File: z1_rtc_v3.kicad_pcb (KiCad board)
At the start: 2 copper layers, 62.5 x 51 mm, 63 parts, among them J1 Conn_01x05, J10 Conn_01x02, J2 61200621621, J3 Conn_01x11, J4 Conn_01x11, J5 Conn_01x11, J6 Conn_01x11, J7 691137710002, J8 USB_B_Micro, J9 Conn_01x02, U1 LCMXO2-1200HC-4SG32C, U2 ATmega328PB-AU, U3 FT230XS, Y1 Crystal_Small

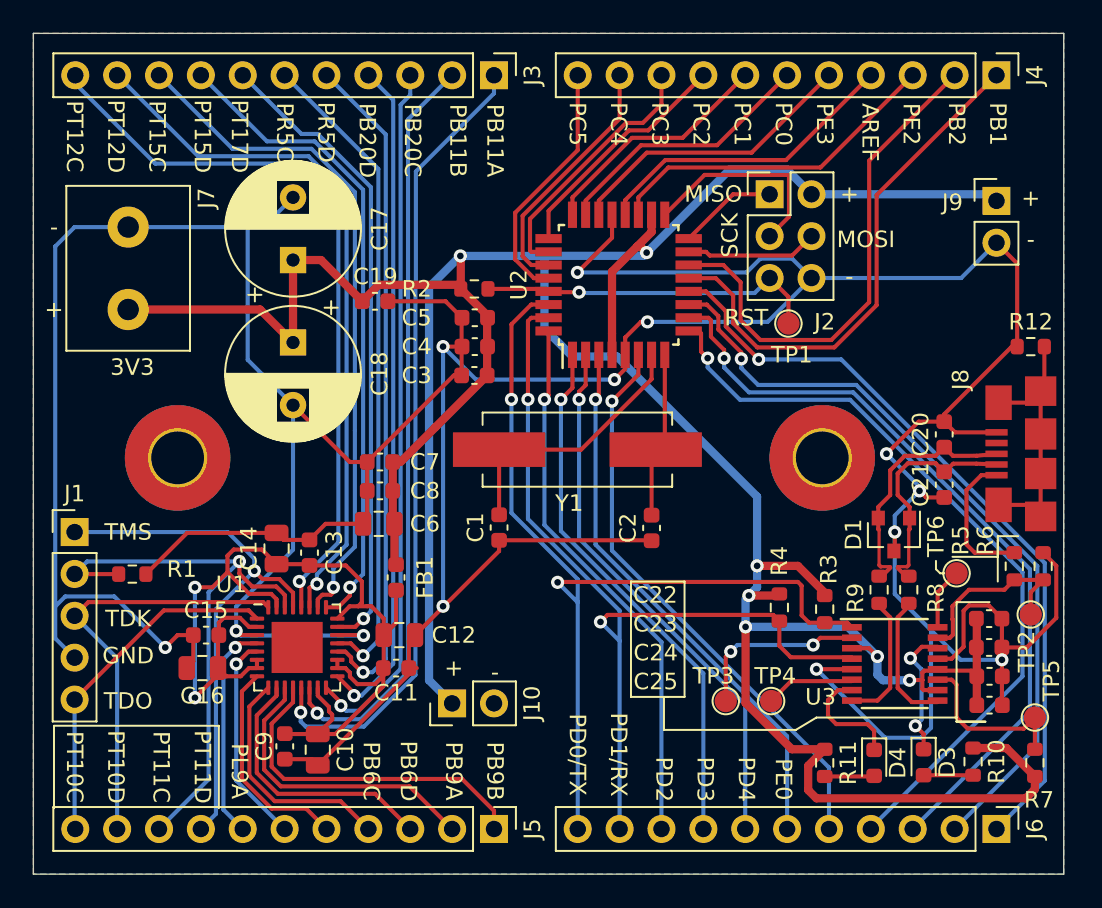
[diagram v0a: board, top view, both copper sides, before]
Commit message: board files for v3.2, with the tinyFPGA module
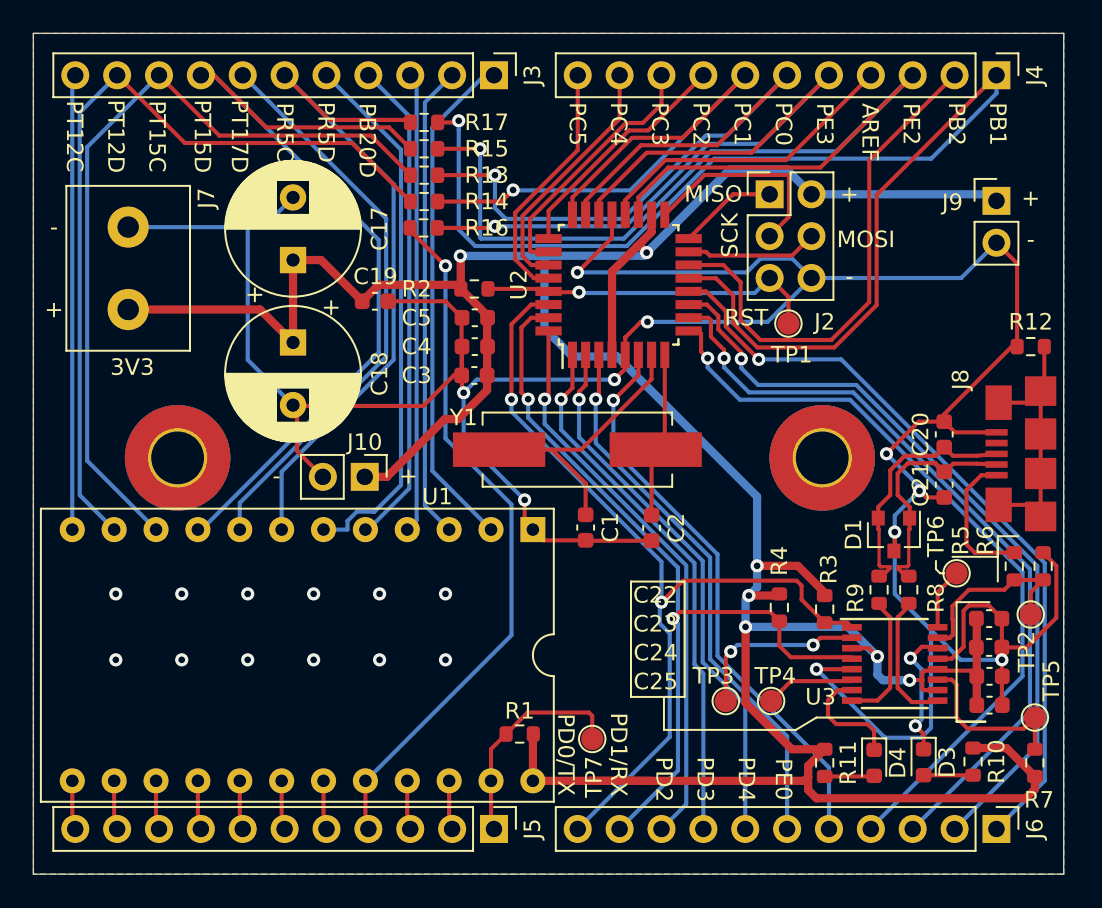
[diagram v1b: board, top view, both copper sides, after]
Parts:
- removed  : MountingHole_3.2mm_M3_Pad_TopBottom, MountingHole:MountingHole_3.2mm_M3_Pad_TopBottom (x2)
- removed C10, C12, C14, C16: 10nF, Capacitor_SMD:C_0805_2012Metric
- removed C11, C13, C15, C8, C9: 0.1uF, Capacitor_SMD:C_0603_1608Metric
- removed C6: 10uF, Capacitor_SMD:C_0805_2012Metric
- removed C7: 1uF, Capacitor_SMD:C_0603_1608Metric
- removed FB1: 33R@100MHz, Capacitor_SMD:C_0603_1608Metric
- removed J1: Conn_01x05, Connector_PinHeader_2.54mm:PinHeader_1x05_P2.54mm_Vertical
- added ?: MountingHole_3.2mm_M3_Pad_TopBottom, MountingHole:MountingHole_3.2mm_M3_Pad_TopBottom, F.Cu at (47.9, 25.8)
- added ?: MountingHole_3.2mm_M3_Pad_TopBottom, MountingHole:MountingHole_3.2mm_M3_Pad_TopBottom, F.Cu at (8.75, 25.8)
- added R13: 0R, Resistor_SMD:R_0603_1608Metric, F.Cu at (23.7, 8.60)
- added R14: 0R, Resistor_SMD:R_0603_1608Metric, F.Cu at (23.7, 10.2)
- added R15: 0R, Resistor_SMD:R_0603_1608Metric, F.Cu at (23.7, 7.00)
- added R16: 0R, Resistor_SMD:R_0603_1608Metric, F.Cu at (23.7, 11.8)
- added R17: 0R, Resistor_SMD:R_0603_1608Metric, F.Cu at (23.7, 5.40)
- added TP7: testpoint_smd_circ, z1_rtc_v3:test_point_smd_circ, F.Cu at (33.9, 42.8)
- R1: value 4.7k -> 10k
- U1: value LCMXO2-1200HC-4SG32C -> tinyFPGA-Ax2; footprint Package_DFN_QFN:QFN-32-1EP_5x5mm_P0.5mm_EP3.1x3.1mm -> z1_rtc_v3:tinyFPGA-Ax2
- moved R1 25.4 mm to (29.5, 42.5), turned to 180 degrees
- moved U1 16.0 mm to (30.3, 30.1), turned to 270 degrees
- moved J10 14.7 mm to (20.1, 26.9), turned to 270 degrees
- moved C1 5.25 mm to (33.5, 30.0)
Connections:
- R1 pad 1: TCK -> +3V3
- R1 pad 2: GND -> PB9B
- U1 pad 1: TDO -> PB11A
- U1 pad 10: PB6D -> PT12D
- U1 pad 11: PB9A -> PT12C
- U1 pad 12: PB9B -> TDO
- U1 pad 13: PB11A -> TDI
- U1 pad 14: PB11B -> TCK
- U1 pad 15: +3.3VP -> TMS
- U1 pad 16: PB20C -> PL9A
- U1 pad 17: PB20D -> PL9B
- U1 pad 18: +3.3VP -> PB4C
- U1 pad 19: +3.3VP -> PB6C
- U1 pad 2: +3.3VP -> PB11B
- U1 pad 20: PR5D -> PB6D
- U1 pad 21: PR5C -> PB9A
- U1 pad 22: GND -> PB9B
- U1 pad 23: PT17D -> +3V3
- U1 pad 3: GND -> PB20C
- U1 pad 4: PL9A -> PB20D
- U1 pad 5: PL9B -> PR5D
- U1 pad 6: +3.3VP -> PR5C
- U1 pad 7: +3.3VP -> PT17D
- U1 pad 8: PB4C -> PT15D
- U1 pad 9: PB6C -> PT15C
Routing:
- net GND: track 317.4 -> 203.7 mm, vias 13 -> 22
- net +3.3VP: track 61.8 -> 0.00 mm, vias 2 -> 0
- net PB1: track 32.1 -> 78.0 mm, vias 0 -> 1
- net PE2: track 20.8 -> 59.1 mm, vias 0 -> 1
- net TCK: track 36.0 -> 2.99 mm, vias 1 -> 0
- net TMS: track 33.1 -> 2.99 mm, vias 1 -> 0
- net PB6C: track 14.4 -> 42.8 mm, vias 0 -> 1
- net PE3: track 18.0 -> 45.6 mm, vias 0 -> 1
- net PC0: track 16.2 -> 43.3 mm, vias 0 -> 1
- net TDI: track 26.2 -> 2.99 mm
- net PC1: track 14.6 -> 36.4 mm, vias 0 -> 1
- net TDO: track 21.4 -> 2.99 mm
- net PB11A: track 48.8 -> 30.9 mm, vias 1 -> 0
- net PT12C: track 45.1 -> 27.6 mm, vias 1 -> 0
- net PB11B: track 45.9 -> 28.9 mm, vias 1 -> 0
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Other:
- rule trace_min: 0.2 -> 0.127
- board text added: "z1_rtc v3.2"
- board text removed: "GND"
- board text removed: "PT10C"
- board text removed: "PT10D"
- board text removed: "PT11C"
- board text removed: "PT11D"
- board text removed: "TDK"
- board text removed: "TDO"
- board text removed: "TMS"
